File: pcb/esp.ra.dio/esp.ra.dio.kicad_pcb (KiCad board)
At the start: 2 copper layers, 75 x 28 mm, 26 parts, among them J1 A, J10 UART, J2 B, J3 C, J4 D, J5 START, J6 SELECT, J7 JOY, J8 USB_B_Micro, J9 BATTERY, SW1 RESET, SW2 POWER, SW3 BOOT, U2 VCC, U3 TLV75533PDBV

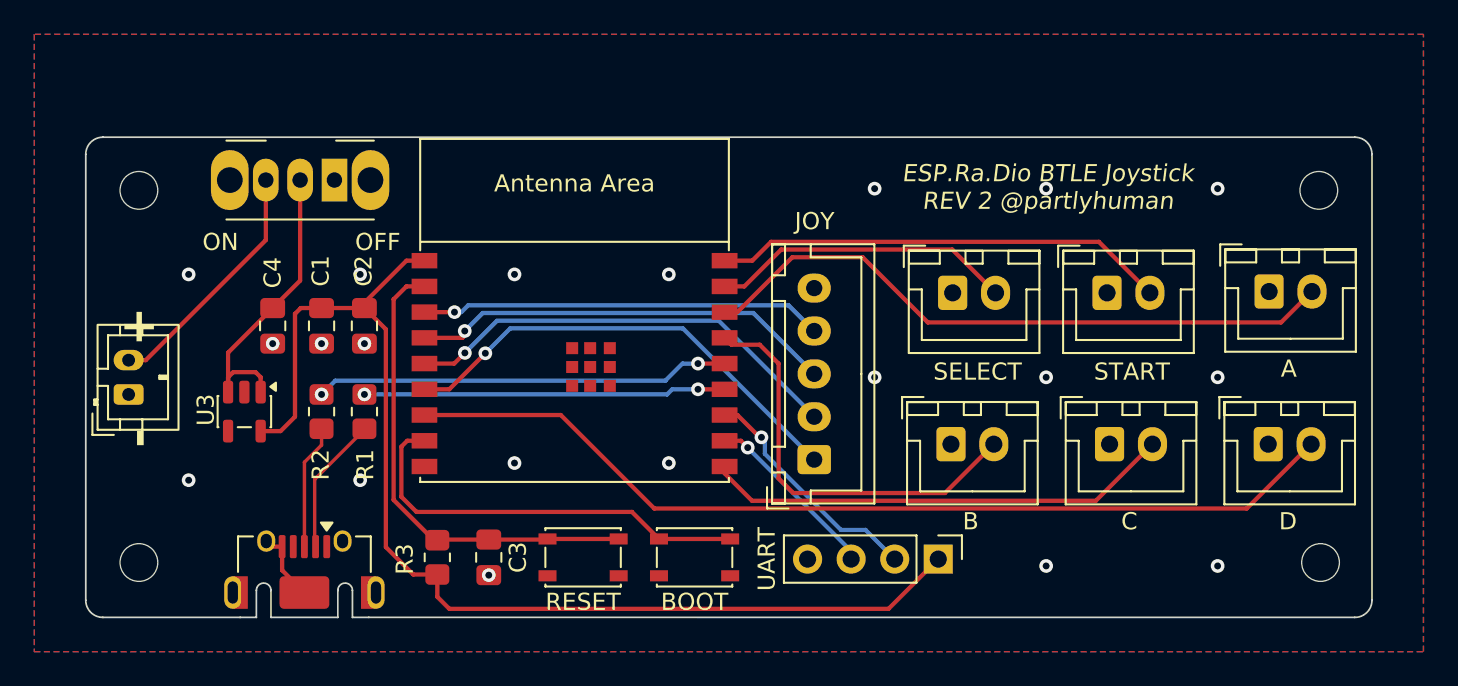
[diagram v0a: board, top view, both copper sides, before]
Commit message: Add activity LED, add weak pullups to strapping pins 2 and 8
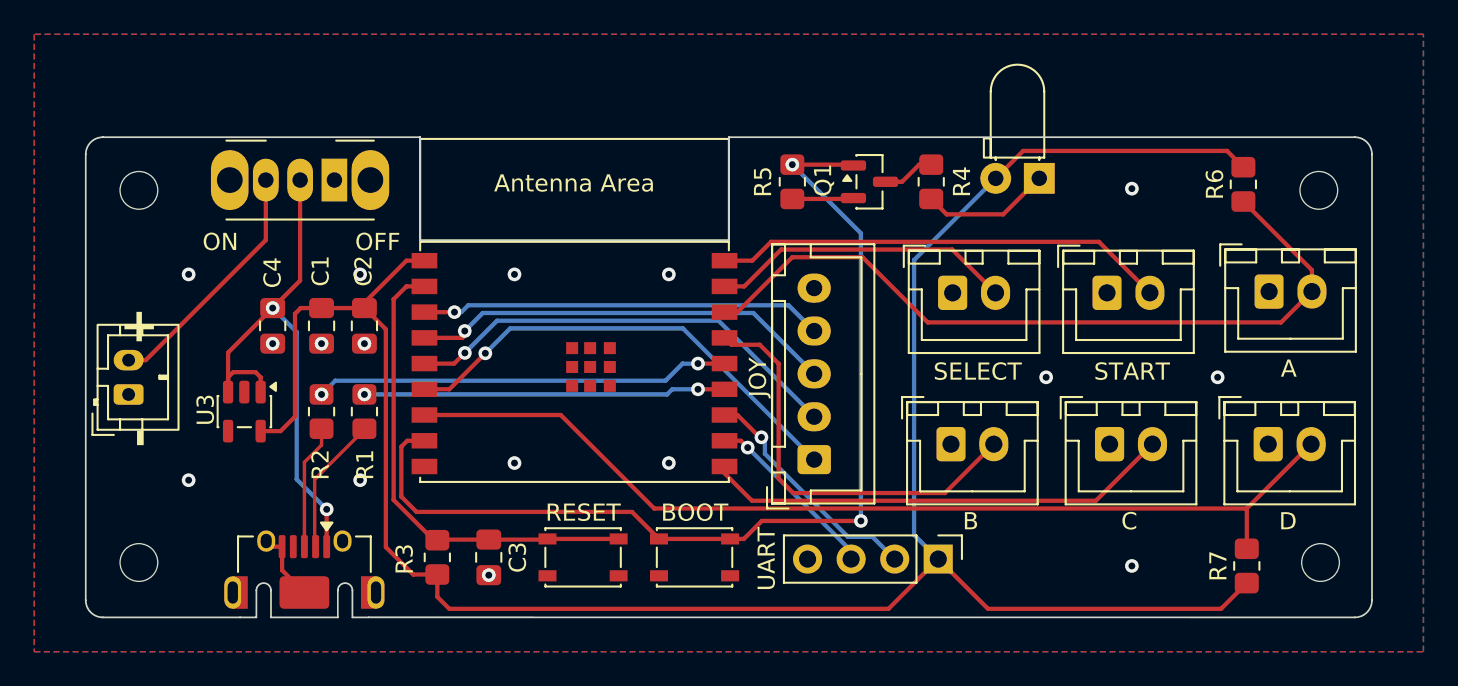
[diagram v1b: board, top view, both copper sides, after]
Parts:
- added D1: LED_Small, LED_THT:LED_D3.0mm_Horizontal_O1.27mm_Z6.0mm, F.Cu at (93.6, 52.4)
- added Q1: BSS138, Package_TO_SOT_SMD:SOT-23, F.Cu at (83.7, 52.6)
- added R4: 4.7K, Resistor_SMD:R_0805_2012Metric_Pad1.20x1.40mm_HandSolder, F.Cu at (87.3, 52.6)
- added R5: 1M, Resistor_SMD:R_0805_2012Metric_Pad1.20x1.40mm_HandSolder, F.Cu at (79.2, 52.6)
- added R6: 1M, Resistor_SMD:R_0805_2012Metric_Pad1.20x1.40mm_HandSolder, F.Cu at (105.5, 52.8)
- added R7: 1M, Resistor_SMD:R_0805_2012Metric_Pad1.20x1.40mm_HandSolder, F.Cu at (105.7, 75.0)
- C3: value 1uF -> 0.1uF
- R3: value 10K -> 1M
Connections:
- net Net-(U2-GPIO9) renamed /GPIO9
- C4 pad 1: /VIN -> /VBUS
- J8 pad 1: unconnected-(J8-VBUS-Pad1) -> /VBUS
- SW2 pad 1: GND -> unconnected-(SW2-A-Pad1)
- SW2 pad 2: /VIN -> /VBUS
- U3 pad 1: /VIN -> /VBUS
- U3 pad 3: /VIN -> /VBUS
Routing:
- net VCC: track 67.5 -> 127.6 mm
- net /GPIO9: track 24.6 -> 58.7 mm, vias 0 -> 2
- net /VBUS: track 0.00 -> 33.2 mm, vias 0 -> 2
- net /VIN: track 18.0 -> 0.00 mm
- net Net-(D1-K): track 0.00 -> 7.54 mm
- net /BA: track 37.9 -> 44.8 mm
- net GND: track 4.27 -> 7.86 mm, vias 20 -> 16
- net Net-(Q1-D): track 0.00 -> 3.08 mm
- net /BD: track 55.5 -> 57.9 mm
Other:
- outline, holes or cut-outs redrawn

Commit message: Comments and cleanup of routing
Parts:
- moved R7 14.2 mm to (91.5, 74.6)
- moved R6 8.70 mm to (96.8, 52.6)
- moved J5 0.19 mm to (97.7, 59.0)
- moved J6 0.13 mm to (88.5, 59.0)
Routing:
- net VCC: track 127.6 -> 101.7 mm
- net /BD: track 57.9 -> 71.0 mm
- net GND: track 7.86 -> 20.7 mm, vias 16 -> 18
- net /BA: track 44.8 -> 51.6 mm
- net /BB: track 24.6 -> 25.1 mm
- net /SEL: track 17.7 -> 18.3 mm
- net /STA: track 26.5 -> 27.0 mm
- net /BC: track 27.4 -> 27.9 mm

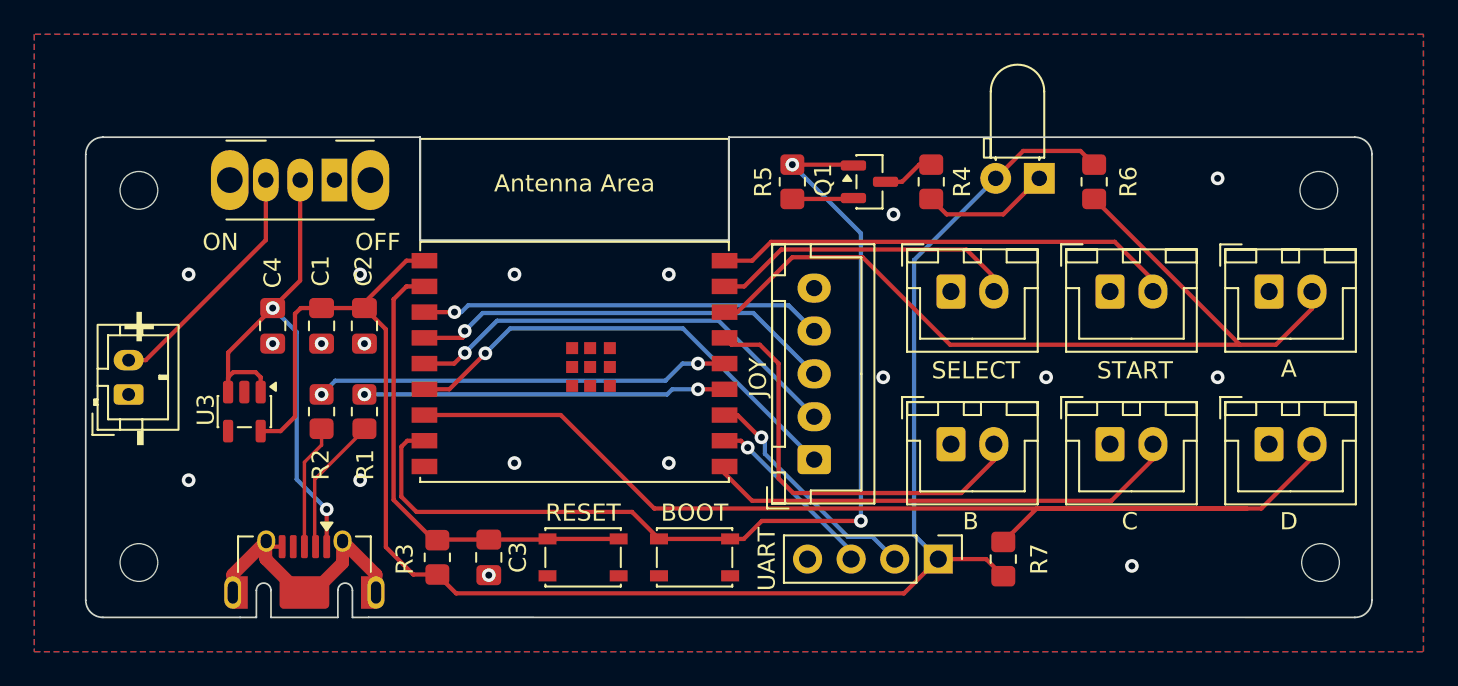
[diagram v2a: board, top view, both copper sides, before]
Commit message: Fix strapping pins, move buttons doubling with strapping pins to TX/RX
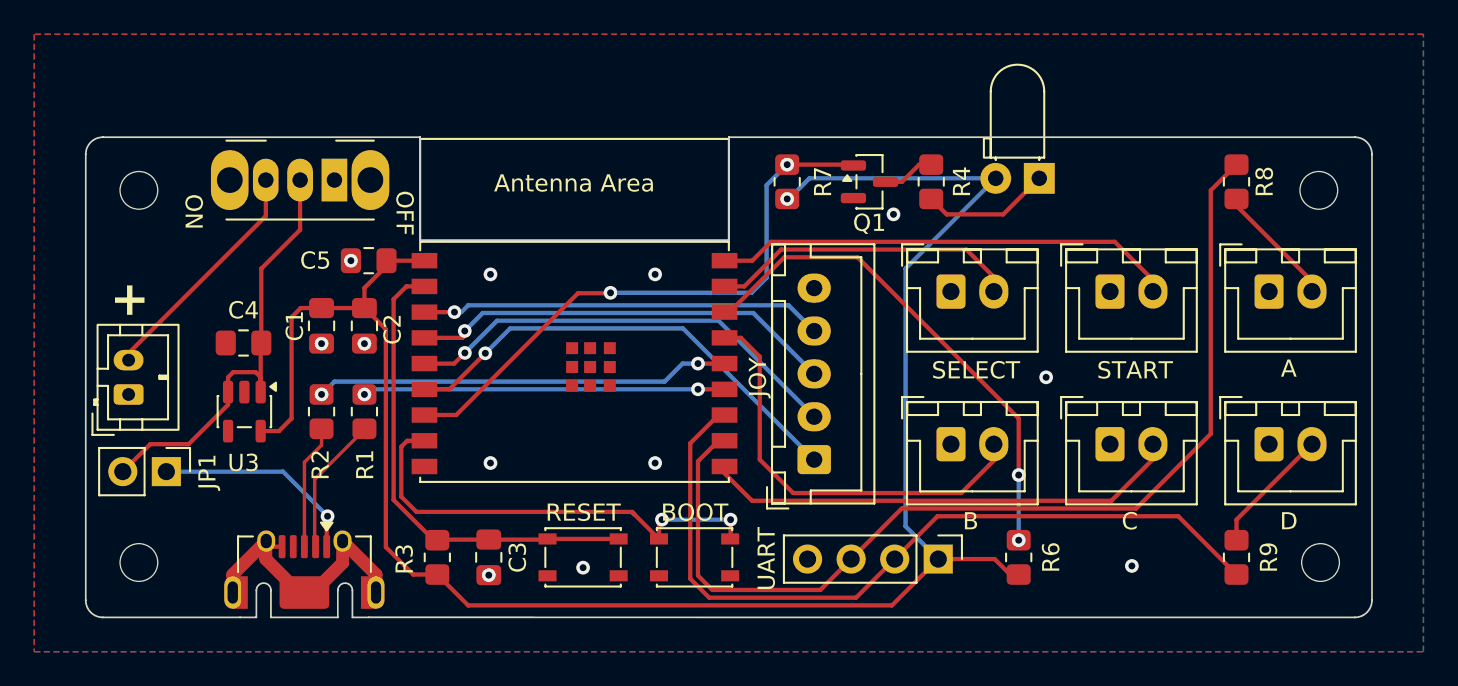
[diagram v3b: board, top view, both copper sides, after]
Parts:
- removed R5: 1M, Resistor_SMD:R_0805_2012Metric_Pad1.20x1.40mm_HandSolder
- added C5: 0.1uF, Capacitor_SMD:C_0805_2012Metric_Pad1.18x1.45mm_HandSolder, F.Cu at (54.5, 57.2)
- added JP1: USB Power, Connector_PinHeader_2.54mm:PinHeader_1x02_P2.54mm_Vertical, F.Cu at (42.7, 69.5)
- added R8: 1K, Resistor_SMD:R_0805_2012Metric_Pad1.20x1.40mm_HandSolder, F.Cu at (105.1, 52.6)
- added R9: 1K, Resistor_SMD:R_0805_2012Metric_Pad1.20x1.40mm_HandSolder, F.Cu at (105.1, 74.5)
- C2: value 0.1uF -> 1uF
- D1: value LED_Small -> ACTLED
- R3: value 1M -> 100K
- moved R7 25.4 mm to (78.9, 52.6)
- moved R6 22.3 mm to (92.4, 74.5), turned to -90 degrees
- moved C4 1.97 mm to (47.2, 62.0), turned to 180 degrees
- renumbered SW2 to SW1, SW1 to SW2
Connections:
- C4 pad 1: /VBUS -> Net-(JP1-B)
- Q1 pad 1: /GPIO9 -> /ACTLED
- R6 pad 1: /BA -> /GPIO2
- R7 pad 2: /BD -> /ACTLED
- SW1 pad 2: /VBUS -> Net-(JP1-B)
- SW3 pad 1: /GPIO9 -> /~{BOOT}
- U2 pad 16: /BA -> /GPIO2
- U2 pad 7: /BD -> /ACTLED
- U2 pad 8: /GPIO9 -> /~{BOOT}
- U3 pad 1: /VBUS -> Net-(JP1-B)
- U3 pad 3: /VBUS -> Net-(JP1-B)
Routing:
- net /BD: track 71.0 -> 7.42 mm
- net /GPIO9: track 58.7 -> 0.00 mm, vias 2 -> 0
- net /RXD: track 10.5 -> 59.0 mm, vias 1 -> 0
- net /BA: track 51.6 -> 7.22 mm
- net /ACTLED: track 0.00 -> 34.2 mm, vias 0 -> 2
- net /TXD: track 13.8 -> 46.3 mm, vias 1 -> 0
- net /GPIO2: track 0.00 -> 29.5 mm, vias 0 -> 2
- net /~{BOOT}: track 0.00 -> 27.0 mm, vias 0 -> 2
- net Net-(JP1-B): track 0.00 -> 25.0 mm
- net /VBUS: track 33.2 -> 12.3 mm, vias 2 -> 1
- net VCC: track 101.7 -> 110.1 mm, vias 0 -> 1
- net GND: track 20.7 -> 17.1 mm, vias 18 -> 12
- net /VBAT: track 14.4 -> 13.8 mm
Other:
- board text added: "+"
- board text removed: "- +"

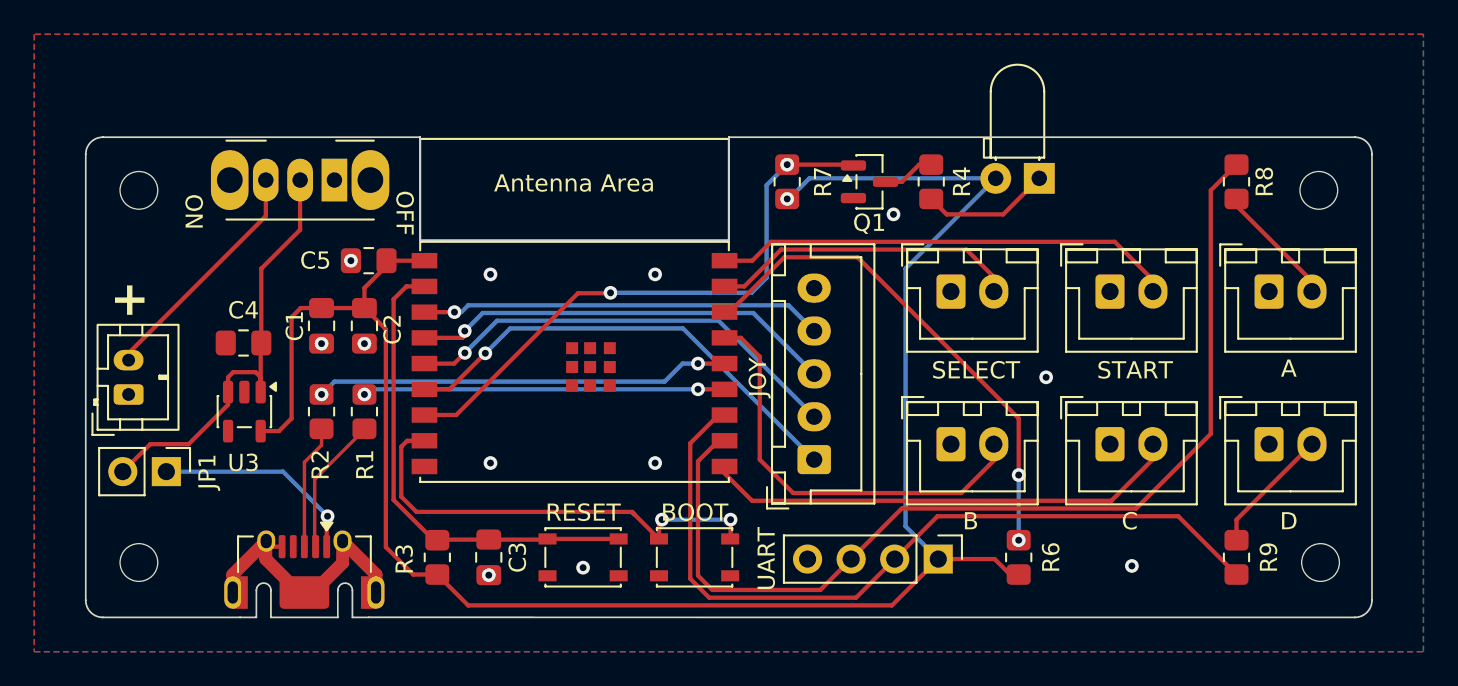
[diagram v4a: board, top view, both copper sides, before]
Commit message: PCB rev fixing do-nothing misplaced resistors
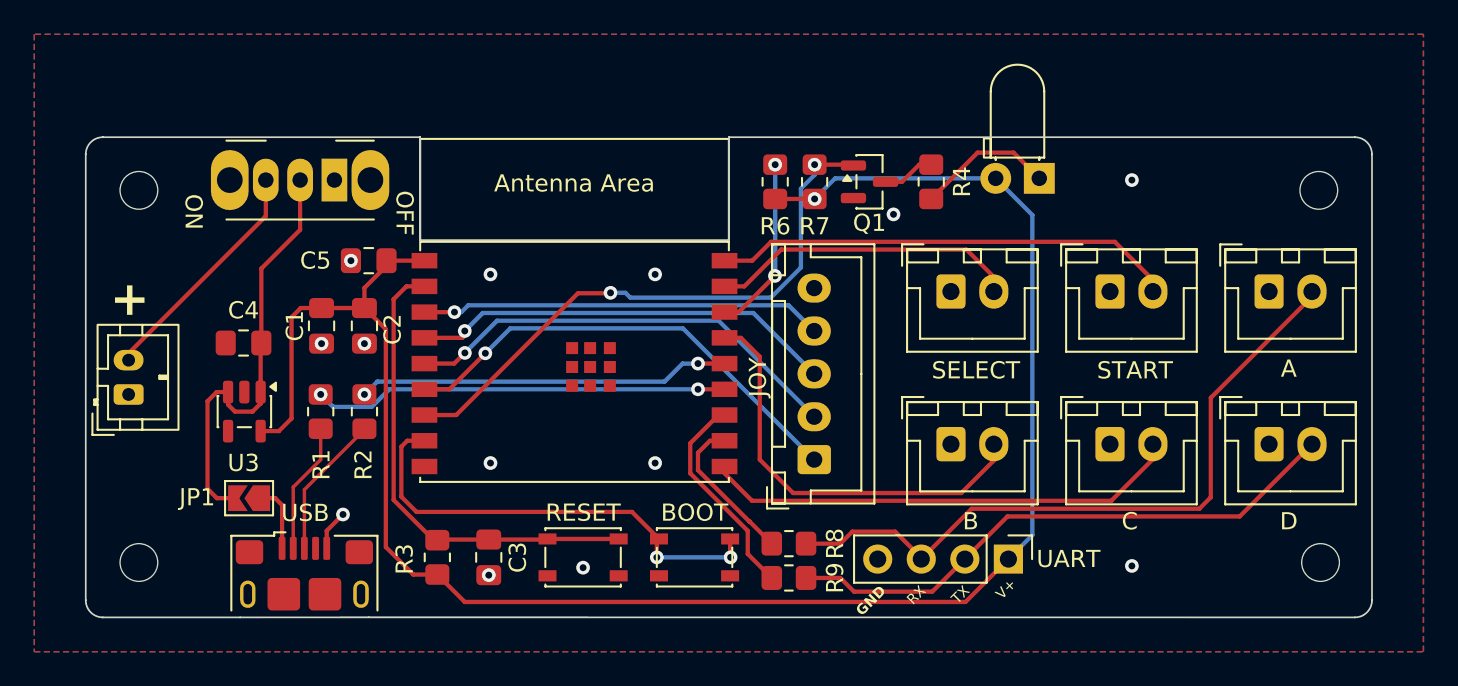
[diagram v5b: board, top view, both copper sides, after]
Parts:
- J8: footprint Connector_USB:USB_Micro-AB_Molex_47590-0001 -> Connector_USB:USB_Micro-B_Amphenol_10118193-0002LF_Horizontal
- JP1: footprint Connector_PinHeader_2.54mm:PinHeader_1x02_P2.54mm_Vertical -> Jumper:SolderJumper-2_P1.3mm_Open_TrianglePad1.0x1.5mm
- moved R8 33.6 mm to (79.0, 73.7), turned to 0 degrees
- moved R9 26.1 mm to (79.0, 75.7), turned to 0 degrees
- moved R6 26.1 mm to (78.2, 52.6)
- moved JP1 5.07 mm to (47.5, 71.0), turned to 180 degrees
- moved J10 4.09 mm to (91.8, 74.6)
- moved R1 2.55 mm to (51.7, 66.0)
- moved R2 2.50 mm to (54.2, 66.0)
- moved R7 1.60 mm to (80.5, 52.6)
- moved J8 0.25 mm to (50.8, 76.7)
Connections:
- J1 pad 2: /BA -> /RX/BA
- J10 pad 2: /TXD -> /TX/BD
- J10 pad 3: /RXD -> /RX/BA
- J4 pad 2: /BD -> /TX/BD
- R8 pad 1: /RXD -> Net-(U2-GPIO20/U0RXD)
- R8 pad 2: /BA -> /RX/BA
- R9 pad 1: /TXD -> Net-(U2-GPIO21/U0TXD)
- R9 pad 2: /BD -> /TX/BD
- U2 pad 11: /RXD -> Net-(U2-GPIO20/U0RXD)
- U2 pad 12: /TXD -> Net-(U2-GPIO21/U0TXD)
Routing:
- net /RXD: track 59.0 -> 0.00 mm
- net /TXD: track 46.3 -> 0.00 mm
- net /RX/BA: track 0.00 -> 40.5 mm
- net /TX/BD: track 0.00 -> 33.4 mm
- net /GPIO2: track 29.5 -> 10.3 mm
- net GND: track 17.1 -> 2.37 mm, vias 12 -> 13
- net Net-(U2-GPIO21/U0TXD): track 0.00 -> 12.5 mm
- net Net-(U2-GPIO20/U0RXD): track 0.00 -> 8.93 mm
- net /VBUS: track 12.3 -> 3.89 mm, vias 1 -> 0
- net /BD: track 7.42 -> 0.00 mm
- net /BA: track 7.22 -> 0.00 mm
- net Net-(U2-GPIO18/USB_D-): track 21.1 -> 24.3 mm
- net Net-(U2-GPIO19/USB_D+): track 24.2 -> 21.7 mm
- net VCC: track 110.1 -> 108.1 mm
- net /USB_DP: track 7.29 -> 8.42 mm
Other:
- board text added: "GND"
- board text added: "RX"
- board text added: "TX"
- board text added: "USB"
- board text added: "V+"

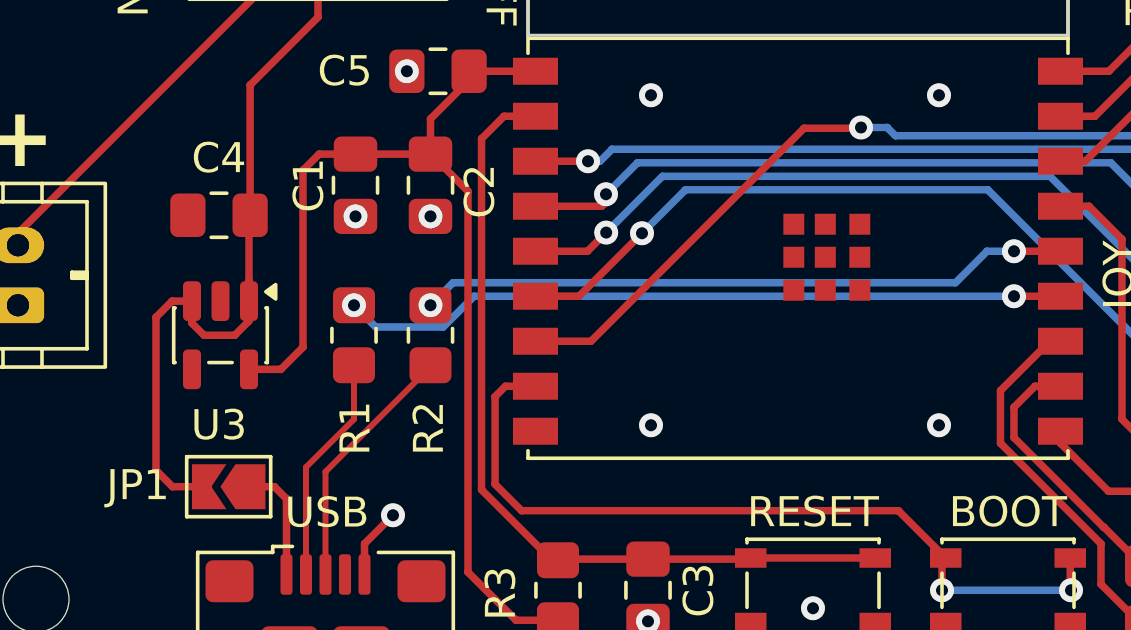
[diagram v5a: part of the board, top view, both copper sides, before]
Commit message: PCB fixes, need to ensure better ground for ldo
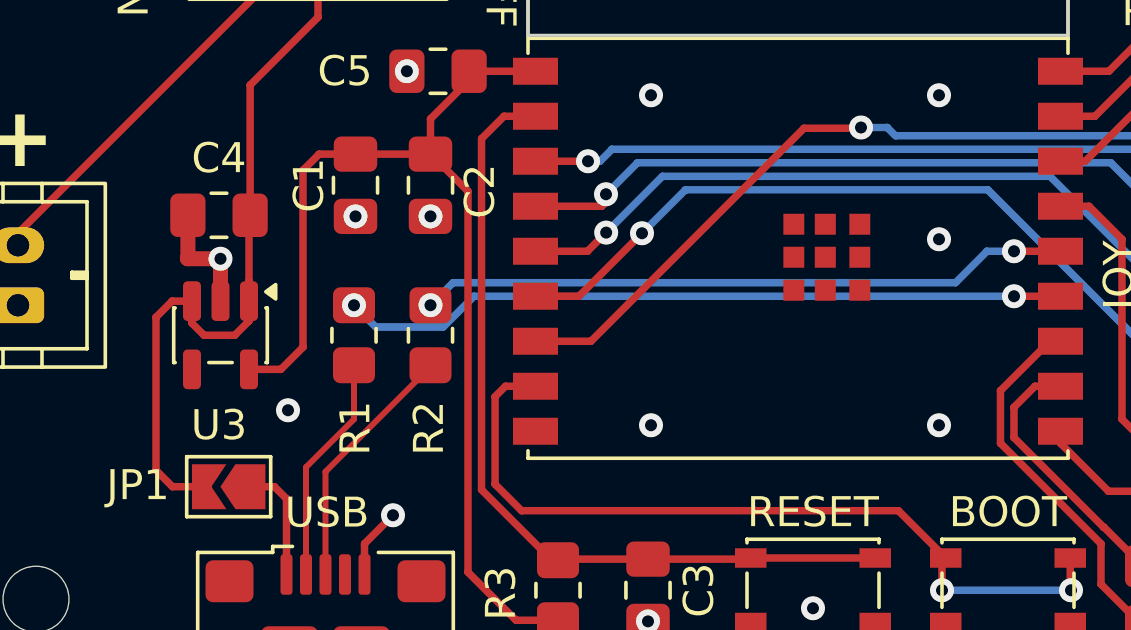
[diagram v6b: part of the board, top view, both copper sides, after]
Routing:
- net GND: track 2.37 -> 6.34 mm, vias 13 -> 16

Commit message: IDK
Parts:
- removed R1, R2: 0R, Resistor_SMD:R_0805_2012Metric_Pad1.20x1.40mm_HandSolder
- added R10: 1M, Resistor_SMD:R_0805_2012Metric_Pad1.20x1.40mm_HandSolder, F.Cu at (82.6, 52.6)
- U3: value TLV75533PDBV -> RT9080-33GJ5
- moved Q1 1.85 mm to (85.5, 52.6), turned to 90 degrees
- moved R4 1.25 mm to (88.5, 52.6)
- moved R7 0.10 mm to (80.4, 52.6)
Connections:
- U2 pad 13: Net-(U2-GPIO18/USB_D-) -> /USB_DN
- U2 pad 14: Net-(U2-GPIO19/USB_D+) -> /USB_DP
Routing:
- net /USB_DN: track 7.64 -> 33.4 mm, vias 0 -> 2
- net /USB_DP: track 8.42 -> 33.4 mm, vias 0 -> 2
- net Net-(U2-GPIO18/USB_D-): track 24.3 -> 0.00 mm, vias 2 -> 0
- net Net-(U2-GPIO19/USB_D+): track 21.7 -> 0.00 mm, vias 2 -> 0
- net /ACTLED: track 34.4 -> 37.2 mm
- net /~{BOOT}: track 27.0 -> 24.6 mm, vias 2 -> 0
- net Net-(D1-K): track 8.04 -> 6.21 mm
- net /BB: track 24.7 -> 25.7 mm
- net VCC: track 108.1 -> 107.5 mm
- net GND: vias 16 -> 17
